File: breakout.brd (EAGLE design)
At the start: 43.2 x 14.4 mm, 38 parts, among them J2 1x3 RA Female .1", J3 CORTEX_DEBUG_PTH

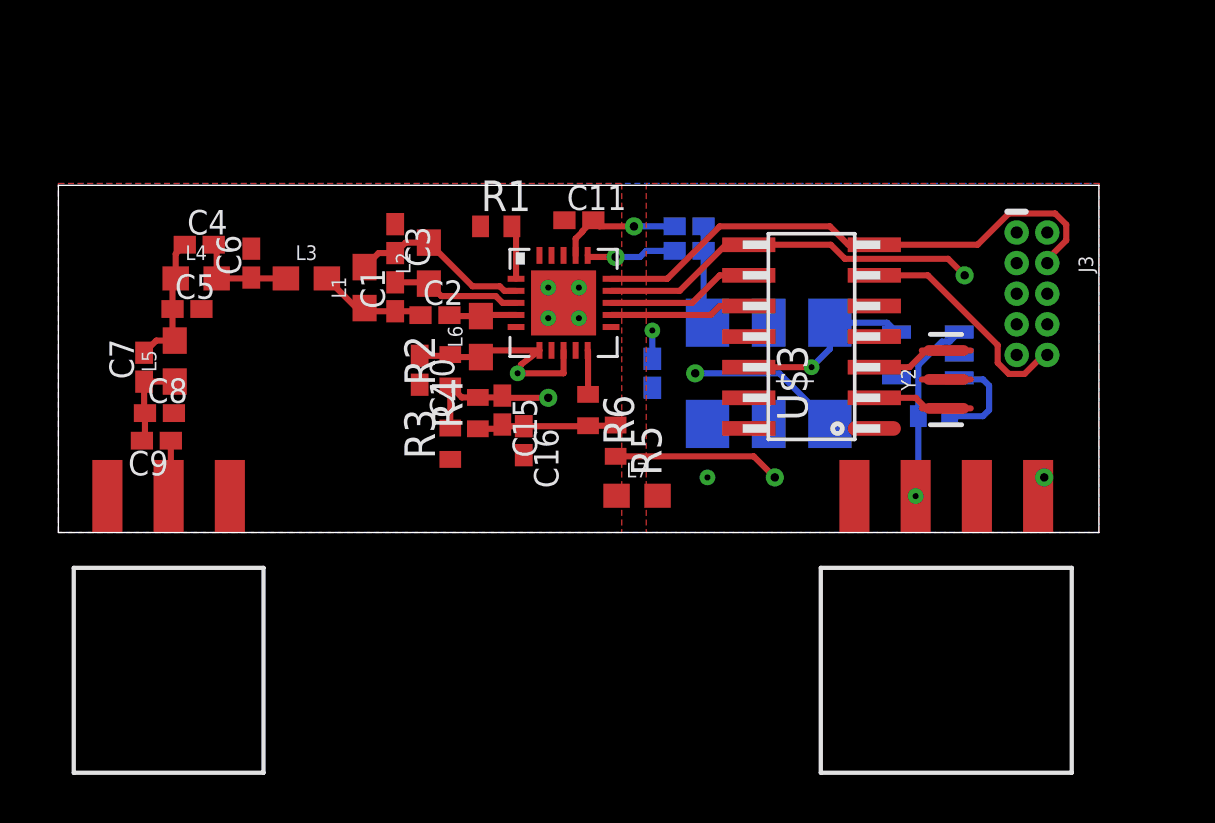
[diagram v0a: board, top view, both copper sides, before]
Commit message: Added SAMD11C14
second routing pass, moved to SAMD11C14 ARM processor
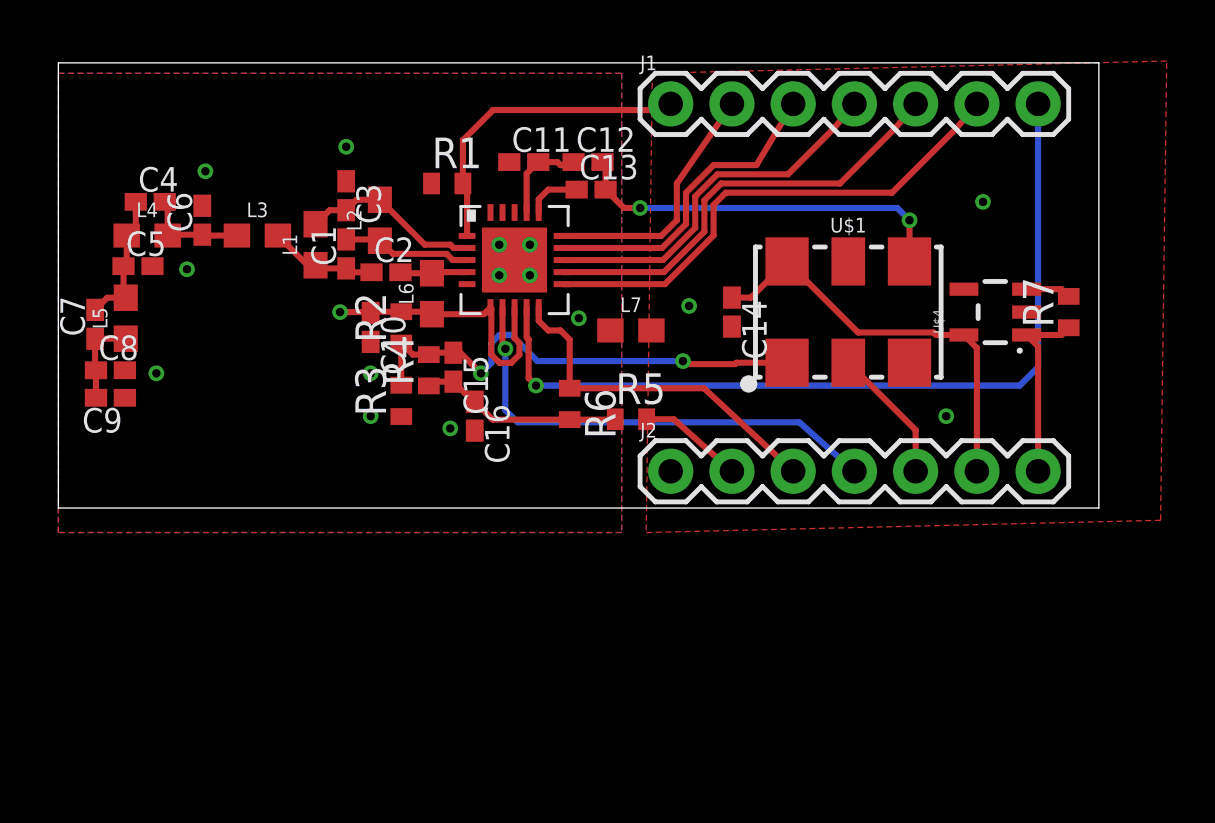
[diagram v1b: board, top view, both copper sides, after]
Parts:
- removed J3: CORTEX_DEBUG_PTH, SparkFun-Connectors:2X5-PTH-1.27MM
- removed U$3: SAMD11C14, atmel_tiny24-44-84tiny48-88mega48-88-168-328:SOIC14
- removed Y2: (no value), SparkFun-Clocks:RESONATOR-SMD-3.2X1.3
- J1: device SparkFun-Connectors:1X04_SMD_RA_FEMALE -> SparkFun-Connectors:1X07
- J2: value 1x3 RA Female .1" -> (none); device SparkFun-Connectors:1X03_SMD_RA_FEMALE -> SparkFun-Connectors:1X07
- moved J1 26.1 mm to (25.4, 17.8)
- moved J2 22.4 mm to (25.4, 2.54)
- moved R7 7.06 mm to (41.9, 9.14), flipped to the top, turned to 90 degrees
- moved L7 6.86 mm to (23.7, 8.38)
- moved C12 4.97 mm to (22.0, 15.4), flipped to the top, turned to 0 degrees
- moved C13 4.79 mm to (22.1, 14.2), flipped to the top, turned to 0 degrees
- moved C14 4.17 mm to (27.9, 9.14), flipped to the top
- moved U$1 4.17 mm to (32.8, 9.14), flipped to the top
- moved C11 3.32 mm to (19.3, 15.4)
- moved U$4 3.31 mm to (38.9, 9.14), flipped to the top, turned to 90 degrees
- moved C1 2.70 mm to (11.9, 11.6)
- moved C10 2.70 mm to (13.0, 8.51)
- moved C2 2.70 mm to (13.6, 10.8)
- moved C3 2.70 mm to (11.9, 14.0)
- moved L1 2.70 mm to (10.7, 11.9)
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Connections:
- removed net !RESET: J3.10, U$3.6
- removed net KEY: J3.7
- removed net MXIN: U$3.2, Y2.1
- removed net MXOUT: U$3.3, Y2.3
- removed net N$17: J3.6
- removed net N$18: J3.8
- removed net PA02: U$3.13
- removed net PA04: U$3.14
- removed net PA05: U$3.1
- removed net PA14: U$3.4
- removed net PA15: U$3.5
- net 5V: now also J2.7; no longer J1.2
- net AUDIO: now also J2.2; no longer J1.4
- net ENABLE: now also J2.5; no longer J1.1
- net GND: no longer J1.3, J2.3, J3.3, J3.5, J3.9, U$3.11, Y2.2
- net GPIO0: now also J1.7
- net MODULATION: now also J2.3
- net NIRQ: now also J1.6
- net PA24: now also J1.4; no longer U$3.9
- net PA25: now also J1.5; no longer U$3.10
- net RADIO_ANT: no longer J2.2
- net RADIO_SDN: now also J1.1
- net SWDCLK: now also J1.2; no longer J3.4, U$3.7
- net SWDIO: now also J1.3; no longer J3.2, U$3.8
- net TXRAMP: now also J2.4
- net VCC: now also J2.6; no longer J3.1, U$3.12
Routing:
- net GPIO0: track 0.00 -> 35.5 mm, vias 0 -> 1
- net NIRQ: track 0.00 -> 21.1 mm
- net TXRAMP: track 0.00 -> 19.8 mm, vias 0 -> 1
- net AUDIO: track 20.7 -> 4.37 mm, vias 2 -> 0
- net MODULATION: track 1.83 -> 14.8 mm
- net PA25: track 5.87 -> 18.4 mm
- net SWDCLK: track 22.7 -> 10.6 mm
- net OUT: track 4.06 -> 16.0 mm, vias 0 -> 2
- net VCC: track 18.2 -> 29.3 mm, vias 3 -> 1
- net RADIO_SDN: track 2.25 -> 13.2 mm
- net !RESET: track 9.62 -> 0.00 mm
- net PA24: track 6.19 -> 15.6 mm
- net SWDIO: track 21.2 -> 13.2 mm, vias 1 -> 0
- net ENABLE: track 0.00 -> 5.66 mm
- net MXOUT: track 3.27 -> 0.00 mm
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- added copper zone on layer 15, net VCC
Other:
- board size 43.2 x 14.4 mm -> 43.2 x 18.5 mm
